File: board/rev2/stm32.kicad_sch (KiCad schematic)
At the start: 1 part, among them U14 STM32G071CBUx

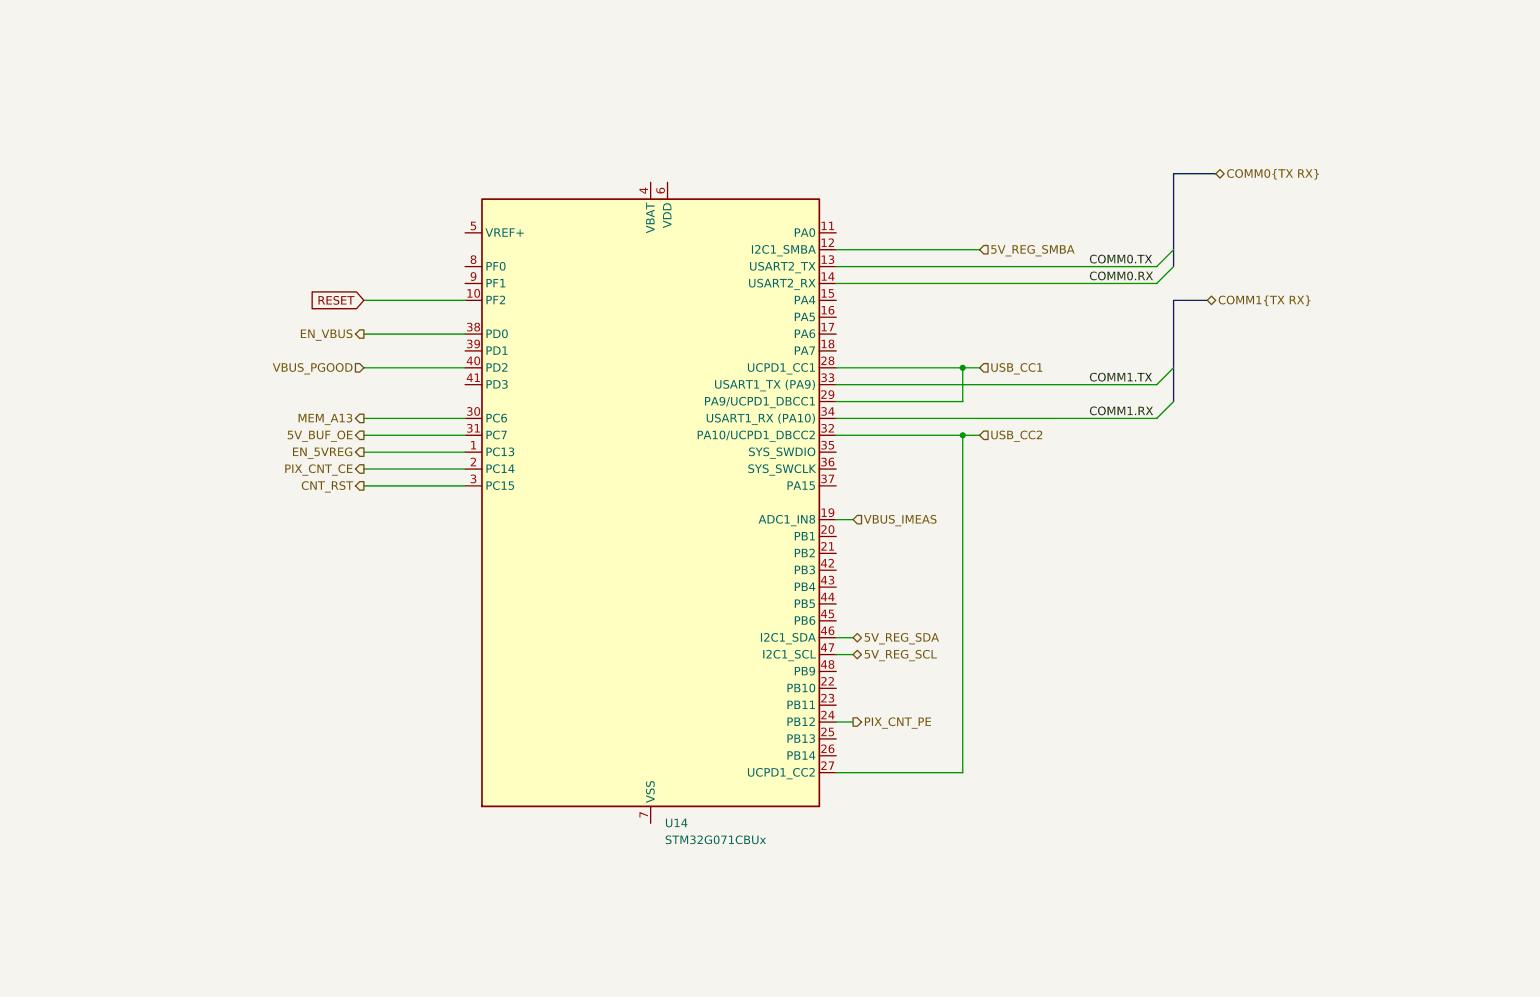
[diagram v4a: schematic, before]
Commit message: Continue board, assign caps/res, adjust for JLC availability
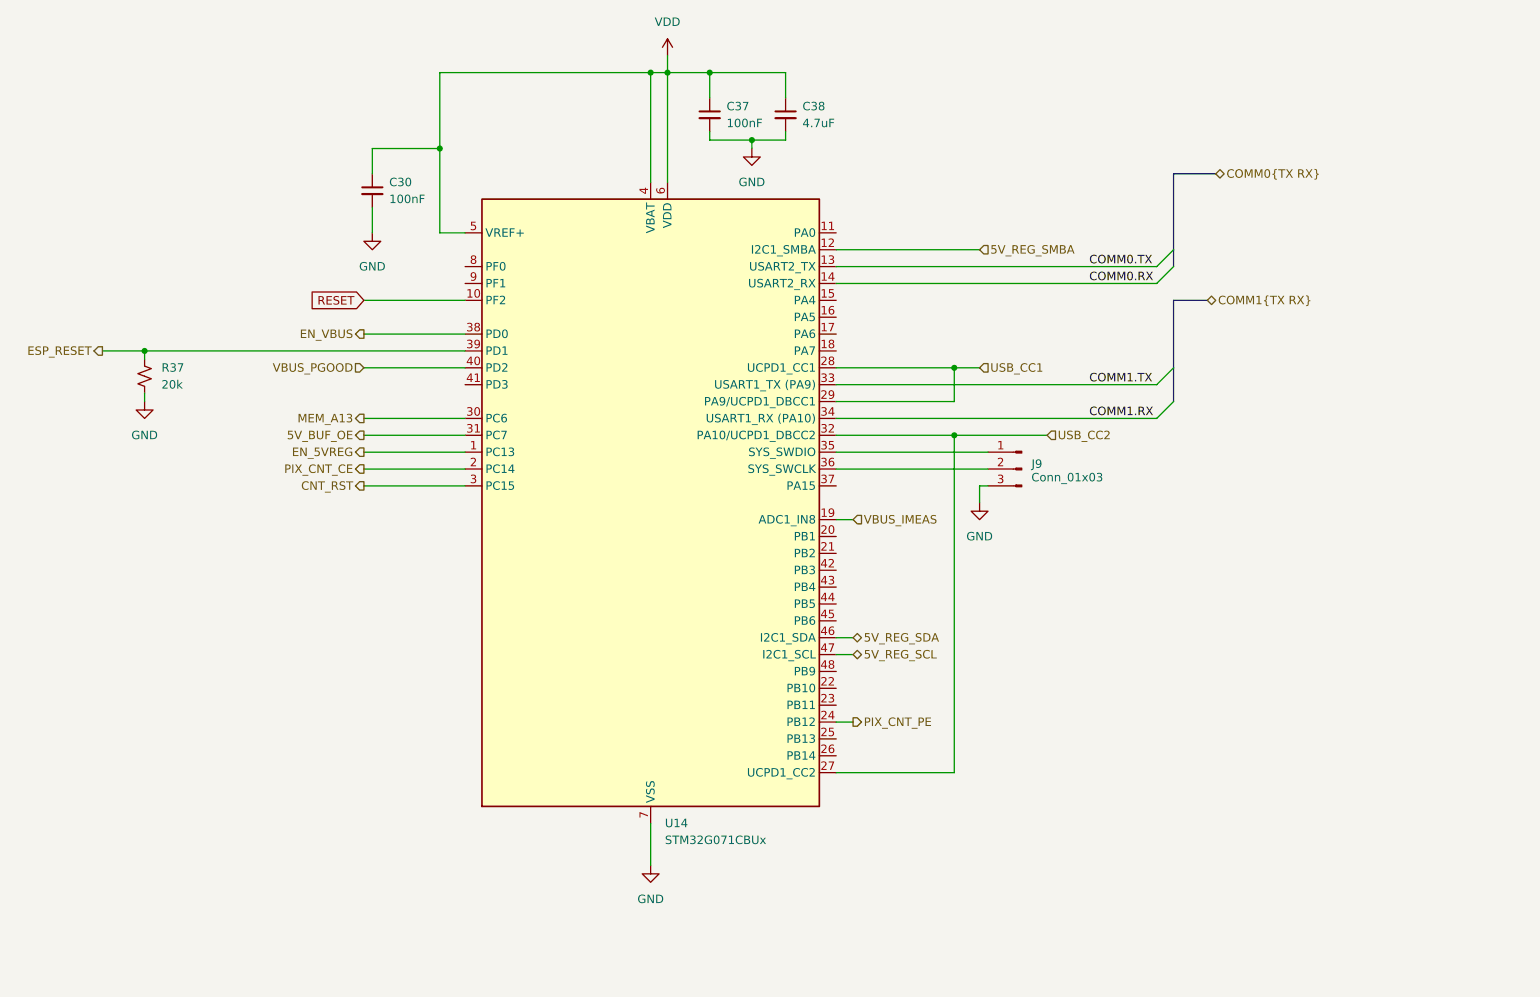
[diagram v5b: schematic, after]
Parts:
- added C30, C37: 100nF, Capacitor_SMD:C_0402_1005Metric, symbol Device:C_Small
- added C38: 4.7uF, Capacitor_SMD:C_1206_3216Metric, symbol Device:C_Small
- added J9: Conn_01x03, Connector_PinHeader_2.54mm:PinHeader_1x03_P2.54mm_Vertical, symbol Connector:Conn_01x03_Pin
- added R37: 20k, Resistor_SMD:R_0603_1608Metric, symbol Device:R_Small_US
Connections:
- net at U14.35 (PA13): now also J9.1 (Pin_1)
- net at U14.36 (PA14): now also J9.2 (Pin_2)
- net ESP_RESET: now reaches U14.39 (PD1)
- net ESP_RESET: now also R37.2
- net VDD: now reaches U14.4 (VBAT)
- net VDD: now also U14.5 (VREF+), U14.6 (VDD), C30.1, C37.1, C38.1
- net GND: now reaches U14.49 (VSS), U14.7 (VSS)
- net GND: now also C30.2, C37.2, C38.2, J9.3 (Pin_3), R37.1

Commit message: Start new PCB
- all footprints setup
- need to setup netclasses next, tho
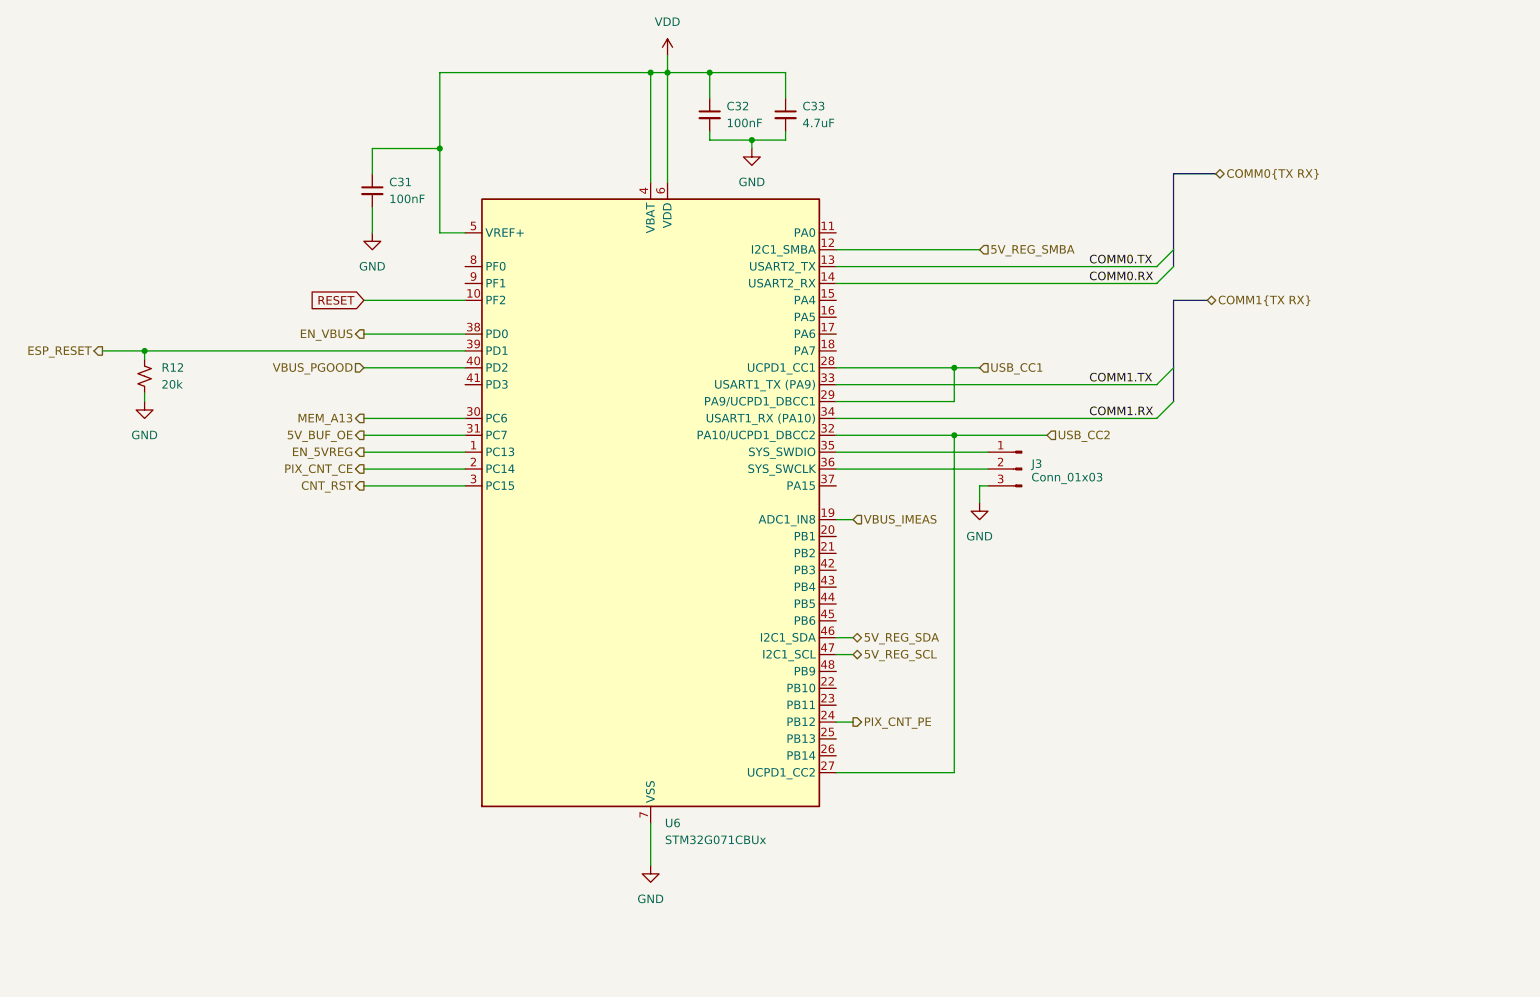
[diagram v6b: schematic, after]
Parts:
- U6: renamed from U14; Part (none) -> STM32G071CBUx
- renumbered C30 to C31, C37 to C32, C38 to C33, J9 to J3, R37 to R12
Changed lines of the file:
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@@
 		(dnp no)
 		(fields_autoplaced yes)
-		(property "Reference" "#PWR059"
+		(property "Reference" "#PWR017"
 			(at 180.34 104.14 0)
 			(effects
@@
 			(project ""
 				(path "/32eb05c7-b4a6-42f3-8fb3-43453631100f/4f7f35d0-2952-4294-913c-05f668985375"
-					(reference "#PWR059")
+					(reference "#PWR017")
 					(unit 1)
 				)
@@
 		(dnp no)
 		(fields_autoplaced yes)
-		(property "Reference" "C30"
+		(property "Reference" "C31"
 			(at 91.44 49.5362 0)
 			(effects
@@
 			(project ""
 				(path "/32eb05c7-b4a6-42f3-8fb3-43453631100f/4f7f35d0-2952-4294-913c-05f668985375"
-					(reference "C30")
+					(reference "C31")
 					(unit 1)
 				)
@@
 		(dnp no)
 		(fields_autoplaced yes)
-		(property "Reference" "#PWR049"
+		(property "Reference" "#PWR012"
 			(at 54.61 88.9 0)
 			(effects
@@
 			(project ""
 				(path "/32eb05c7-b4a6-42f3-8fb3-43453631100f/4f7f35d0-2952-4294-913c-05f668985375"
-					(reference "#PWR049")
+					(reference "#PWR012")
 					(unit 1)
 				)
@@
 		(dnp no)
 		(fields_autoplaced yes)
-		(property "Reference" "C38"
+		(property "Reference" "C33"
 			(at 153.67 38.1062 0)
 			(effects
@@
 			(project ""
 				(path "/32eb05c7-b4a6-42f3-8fb3-43453631100f/4f7f35d0-2952-4294-913c-05f668985375"
-					(reference "C38")
+					(reference "C33")
 					(unit 1)
 				)
@@
 		(dnp no)
 		(fields_autoplaced yes)
-		(property "Reference" "R37"
+		(property "Reference" "R12"
 			(at 57.15 77.4699 0)
 			(effects
@@
 			(project ""
 				(path "/32eb05c7-b4a6-42f3-8fb3-43453631100f/4f7f35d0-2952-4294-913c-05f668985375"
-					(reference "R37")
+					(reference "R12")
 					(unit 1)
 				)
@@
 		(dnp no)
 		(fields_autoplaced yes)
-		(property "Reference" "#PWR045"
+		(property "Reference" "#PWR015"
 			(at 133.35 34.29 0)
 			(effects
@@
 			(project ""
 				(path "/32eb05c7-b4a6-42f3-8fb3-43453631100f/4f7f35d0-2952-4294-913c-05f668985375"
-					(reference "#PWR045")
+					(reference "#PWR015")
 					(unit 1)
 				)
@@
 		(on_board yes)
 		(dnp no)
-		(property "Reference" "J9"
+		(property "Reference" "J3"
 			(at 188.976 91.948 0)
 			(effects
@@
 			(project "mainboard"
 				(path "/32eb05c7-b4a6-42f3-8fb3-43453631100f/4f7f35d0-2952-4294-913c-05f668985375"
-					(reference "J9")
+					(reference "J3")
 					(unit 1)
 				)
@@
 		(dnp no)
 		(fields_autoplaced yes)
-		(property "Reference" "#PWR046"
+		(property "Reference" "#PWR013"
 			(at 88.9 63.5 0)
 			(effects
@@
 			(project ""
 				(path "/32eb05c7-b4a6-42f3-8fb3-43453631100f/4f7f35d0-2952-4294-913c-05f668985375"
-					(reference "#PWR046")
+					(reference "#PWR013")
 					(unit 1)
 				)
@@
 		(dnp no)
 		(fields_autoplaced yes)
-		(property "Reference" "C37"
+		(property "Reference" "C32"
 			(at 142.24 38.1062 0)
 			(effects
@@
 			(project ""
 				(path "/32eb05c7-b4a6-42f3-8fb3-43453631100f/4f7f35d0-2952-4294-913c-05f668985375"
-					(reference "C37")
+					(reference "C32")
 					(unit 1)
 				)
@@
 		(dnp no)
 		(fields_autoplaced yes)
-		(property "Reference" "#PWR048"
+		(property "Reference" "#PWR014"
 			(at 130.81 158.75 0)
 			(effects
@@
 			(project ""
 				(path "/32eb05c7-b4a6-42f3-8fb3-43453631100f/4f7f35d0-2952-4294-913c-05f668985375"
-					(reference "#PWR048")
+					(reference "#PWR014")
 					(unit 1)
 				)
@@
 		(dnp no)
 		(fields_autoplaced yes)
-		(property "Reference" "U14"
+		(property "Reference" "U6"
 			(at 132.9533 146.05 0)
 			(effects
@@
 			)
 		)
+		(property "Part" "STM32G071CBUx"
+			(at 130.81 97.79 0)
+			(effects
+				(font
+					(size 1.27 1.27)
+				)
+				(hide yes)
+			)
+		)
 		(pin "47"
 			(alternate "I2C1_SCL")
@@
 			(project ""
 				(path "/32eb05c7-b4a6-42f3-8fb3-43453631100f/4f7f35d0-2952-4294-913c-05f668985375"
-					(reference "U14")
+					(reference "U6")
 					(unit 1)
 				)
@@
 		(dnp no)
 		(fields_autoplaced yes)
-		(property "Reference" "#PWR047"
+		(property "Reference" "#PWR016"
 			(at 146.05 50.8 0)
 			(effects
@@
 			(project ""
 				(path "/32eb05c7-b4a6-42f3-8fb3-43453631100f/4f7f35d0-2952-4294-913c-05f668985375"
-					(reference "#PWR047")
-					(unit 1)
-				)
+					(reference "#PWR016")
+					(unit 1)
+				)

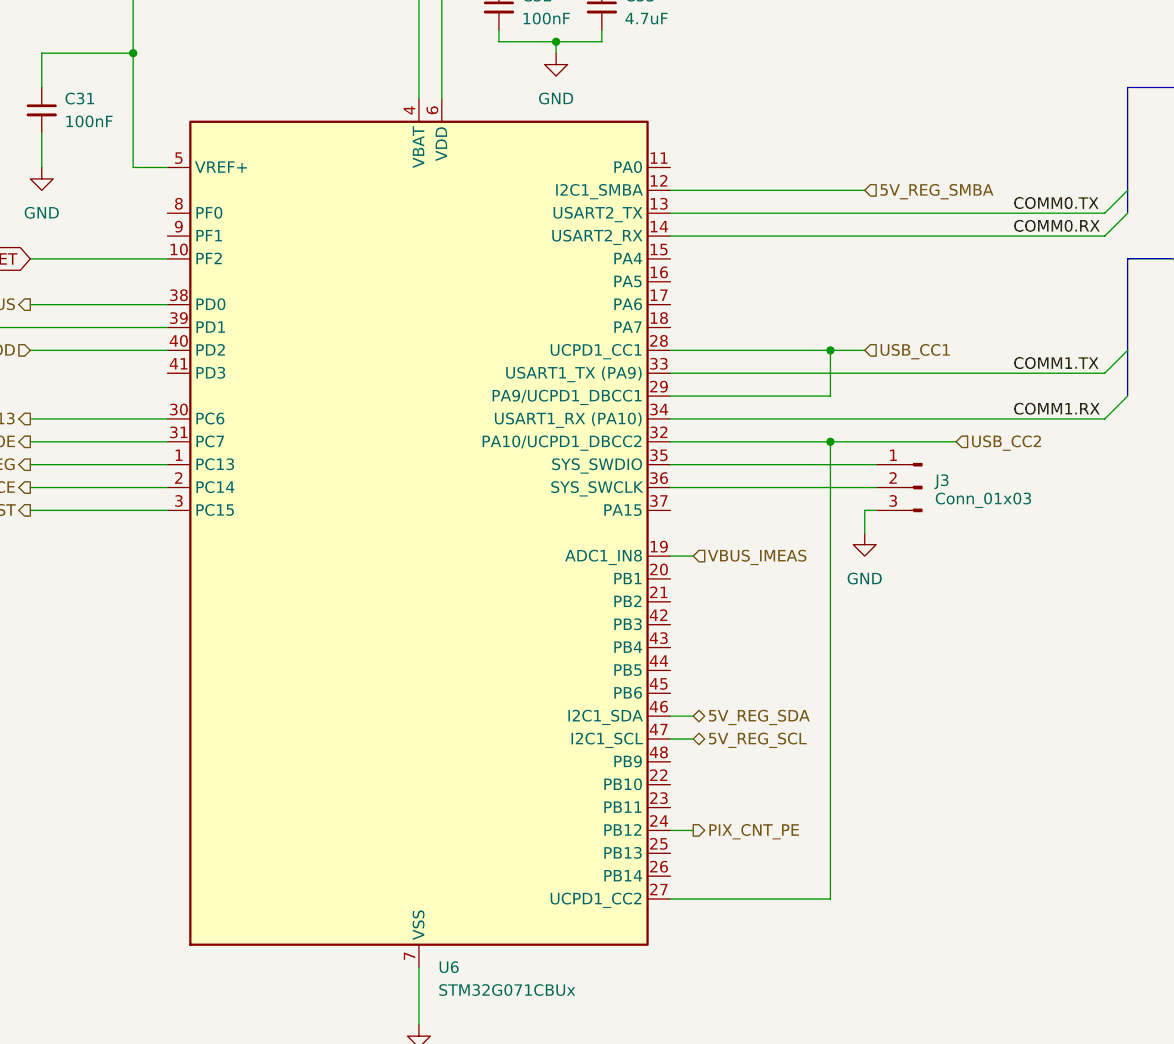
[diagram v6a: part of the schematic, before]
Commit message: Add netclasses, more footprints, fix ERC
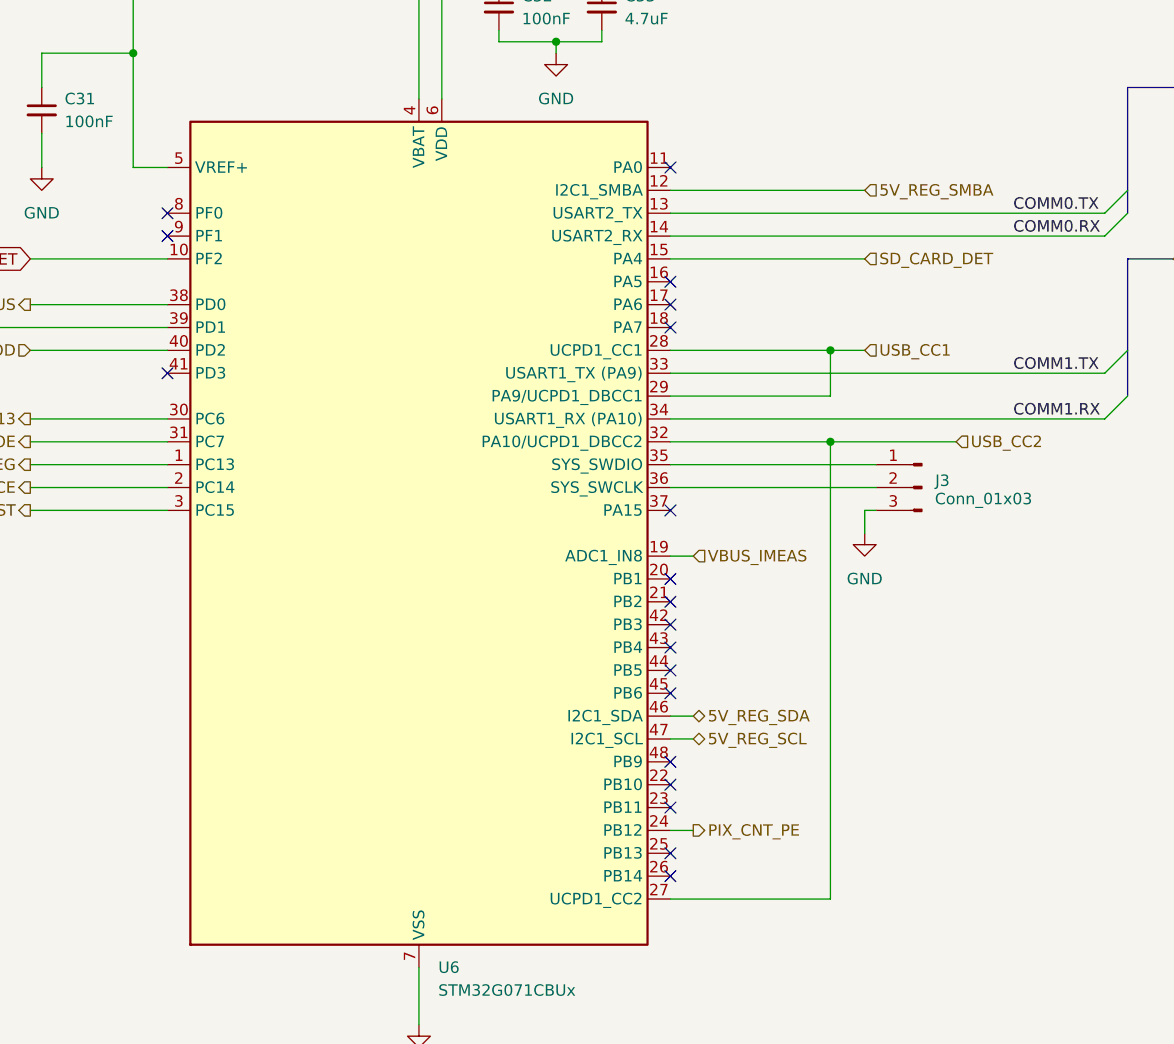
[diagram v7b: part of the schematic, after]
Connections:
- net SD_CARD_DET: now reaches U6.15 (PA4)
- no-connect marks 0 -> 19
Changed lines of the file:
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@@
 		(color 0 0 0 0)
+	)
+	(no_connect
+		(at 158.75 95.25)
+	)
+	(no_connect
+		(at 158.75 57.15)
+	)
+	(no_connect
+		(at 102.87 64.77)
+	)
+	(no_connect
+		(at 158.75 133.35)
+	)
+	(no_connect
+		(at 102.87 62.23)
+	)
+	(no_connect
+		(at 158.75 128.27)
+	)
+	(no_connect
+		(at 158.75 102.87)
+	)
+	(no_connect
+		(at 158.75 72.39)
+	)
+	(no_connect
+		(at 158.75 110.49)
+	)
+	(no_connect
+		(at 102.87 80.01)
+	)
+	(no_connect
+		(at 158.75 135.89)
+	)
+	(no_connect
+		(at 158.75 113.03)
+	)
+	(no_connect
+		(at 158.75 107.95)
+	)
+	(no_connect
+		(at 158.75 115.57)
+	)
+	(no_connect
+		(at 158.75 69.85)
+	)
+	(no_connect
+		(at 158.75 74.93)
+	)
+	(no_connect
+		(at 158.75 123.19)
+	)
+	(no_connect
+		(at 158.75 105.41)
+	)
+	(no_connect
+		(at 158.75 125.73)
 	)
 	(bus_entry
@@
 		(pts
 			(xy 158.75 77.47) (xy 176.53 77.47)
+		)
+		(stroke
+			(width 0)
+			(type default)
+		)
+	)
+	(wire
+		(pts
+			(xy 180.34 67.31) (xy 158.75 67.31)
 		)
 		(stroke
@@
 		(effects
 			(font
+				(size 1.27 1.27)
+			)
+			(justify left)
+		)
+	)
+	(hierarchical_label "SD_CARD_DET"
+		(shape input)
+		(at 180.34 67.31 0)
+		(effects
+			(font
